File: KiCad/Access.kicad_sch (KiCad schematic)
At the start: 59 parts, among them J1 USB-C, J2 RFID, J3 INPUTS, J4 ExtTamper, J5 POWER, J6 DOOR, Q1 NX7002AK, SW1 Tamper, U1 ESP32-WROOM-32, U2 FT231XQ, U3 G3VM-41GR8, U4 LMR16006YQ3, U5 LMR16006YQ3/Q5, U6 AA, U7 QR

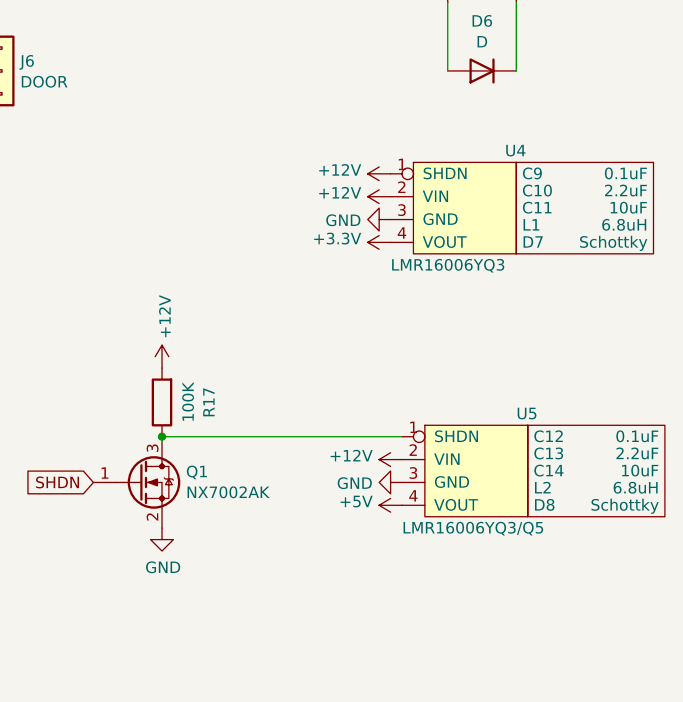
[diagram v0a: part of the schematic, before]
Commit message: More KiCad 6 tweaks
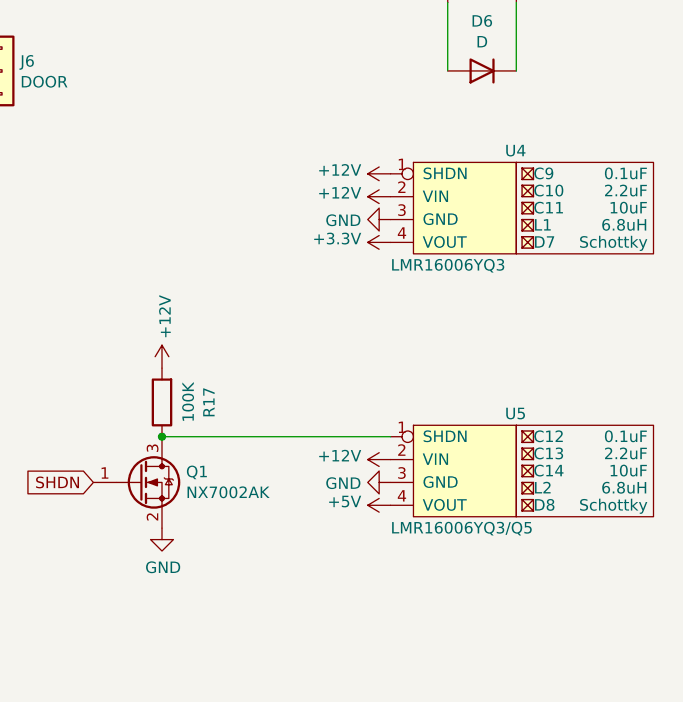
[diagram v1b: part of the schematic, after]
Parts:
- D1, D2, D3, D4: footprint Package_TO_SOT_SMD:SOT-363_SC-70-6 -> RevK:SOT-363_SC-70-6
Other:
- moved on the sheet: U5

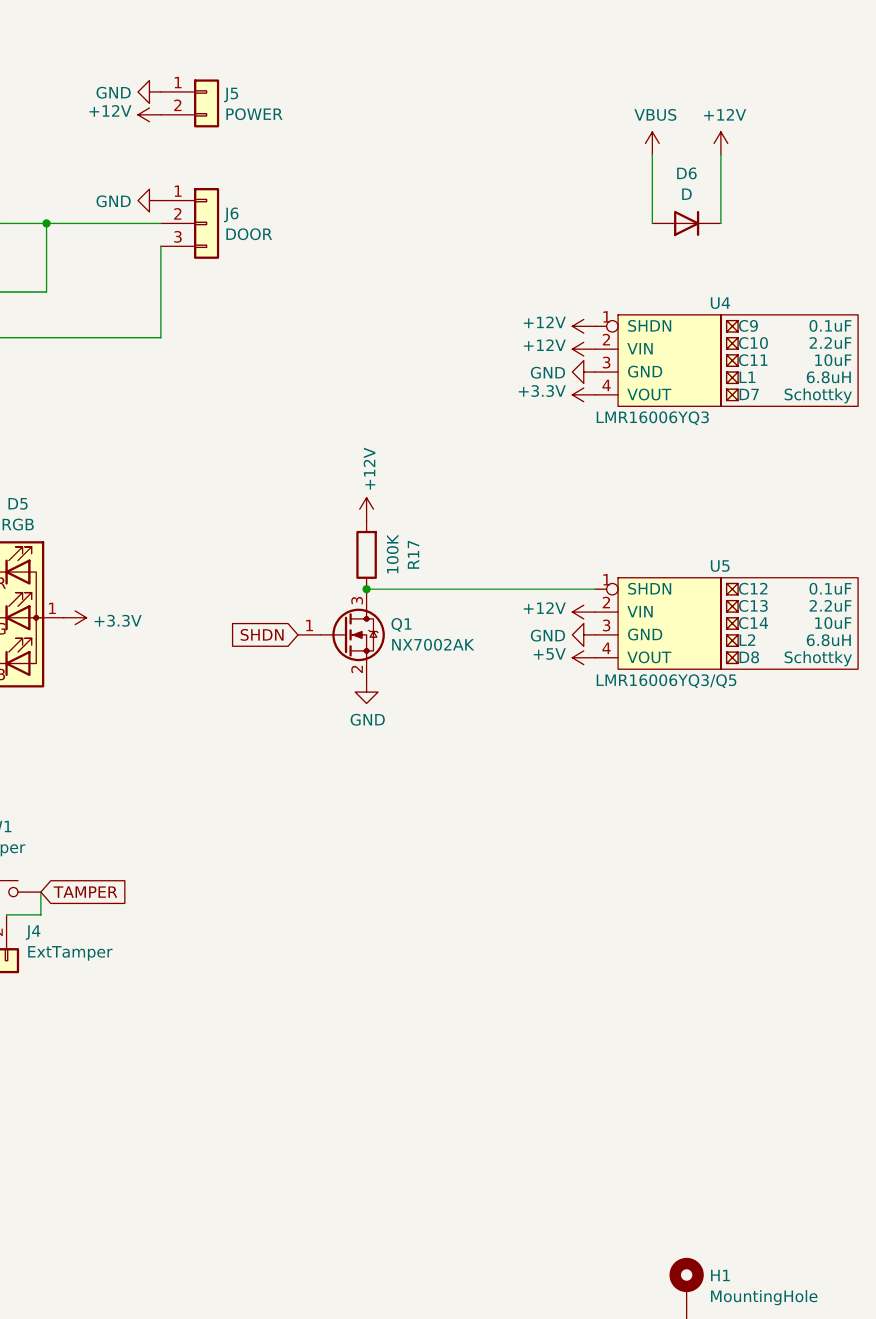
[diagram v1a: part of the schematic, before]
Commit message: Reworked for variable regulators
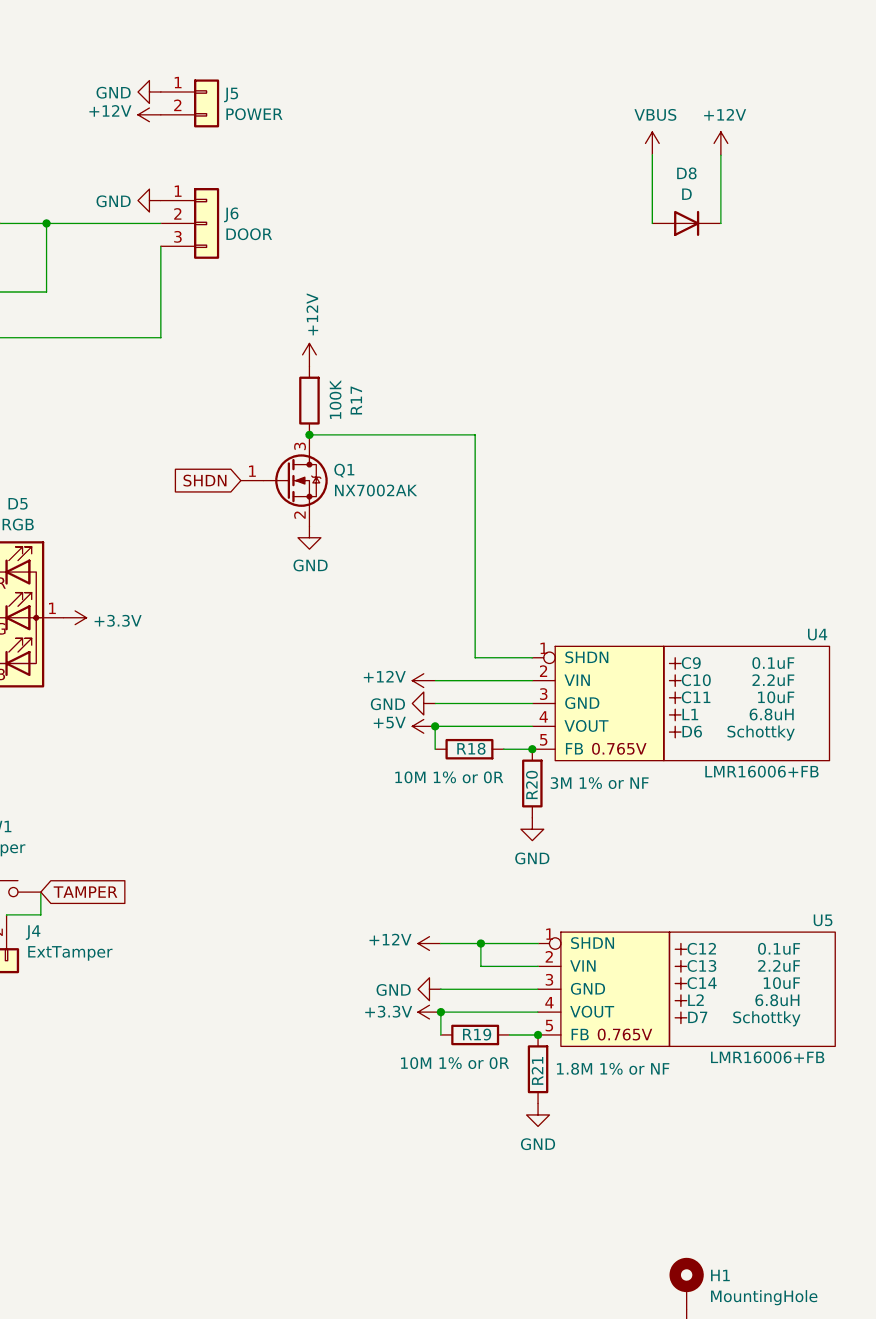
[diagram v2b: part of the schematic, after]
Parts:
- removed U4: LMR16006YQ3, RevK:RegulatorBlock, symbol RevK:LMR16006YQ3
- removed U5: LMR16006YQ3/Q5, RevK:RegulatorBlock, symbol RevK:LMR16006YQ3
- added R18, R19: 10M 1% or 0R, RevK:R_0603, symbol Device:R
- added R20: 3M 1% or NF, RevK:R_0603, symbol Device:R
- added R21: 1.8M 1% or NF, RevK:R_0603, symbol Device:R
- added U4, U5: LMR16006+FB, RevK:RegulatorBlockFB, symbol RevK:LMR16006+FB
- AJK1, U6, U7: Note (none) -> Non part, PCB printed
- D1, D2, D3, D4: footprint RevK:SOT-363_SC-70-6 -> Package_TO_SOT_SMD:SOT-363_SC-70-6
- renumbered C13 to C10, C14 to C11, C9 to C12, C10 to C13, C11 to C14, C12 to C9, D8 to D6, D6 to D8, L2 to L1, L1 to L2
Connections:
- net +12V: now also U4.2 (VIN), U5.1 (SHDN), U5.2 (VIN)
- net +3V3: now also R19.1, U5.4 (VOUT)
- net +5V: now also R18.1, U4.4 (VOUT)
- net GND: now also R20.1, R21.1, U4.3 (GND), U5.3 (GND)
- net at Q1.3 (D), R17.1: now also U4.1 (SHDN)
- new net: R19.2, R21.2, U5.5 (FB)
- new net: R18.2, R20.2, U4.5 (FB)
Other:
- moved on the sheet: Q1, R17

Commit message: Update date, and tidy
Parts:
- U1: footprint RF_Module:ESP32-WROOM-32 -> RevK:ESP32-WROOM-32
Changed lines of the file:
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@@
     (property "Reference" "U1" (id 0) (at 46.99 22.7076 0))
     (property "Value" "ESP32-WROOM-32" (id 1) (at 46.99 25.019 0))
-    (property "Footprint" "RF_Module:ESP32-WROOM-32" (id 2) (at 46.99 100.965 0)
+    (property "Footprint" "RevK:ESP32-WROOM-32" (id 2) (at 46.99 100.965 0)
       (effects (font (size 1.27 1.27)) hide)
     )
@@
     )
     (path "/00000000-0000-0000-0000-00006043326c"
-      (reference "U1") (unit 1) (value "ESP32-WROOM-32") (footprint "RF_Module:ESP32-WROOM-32")
+      (reference "U1") (unit 1) (value "ESP32-WROOM-32") (footprint "RevK:ESP32-WROOM-32")
     )
     (path "/00000000-0000-0000-0000-00006084108b"

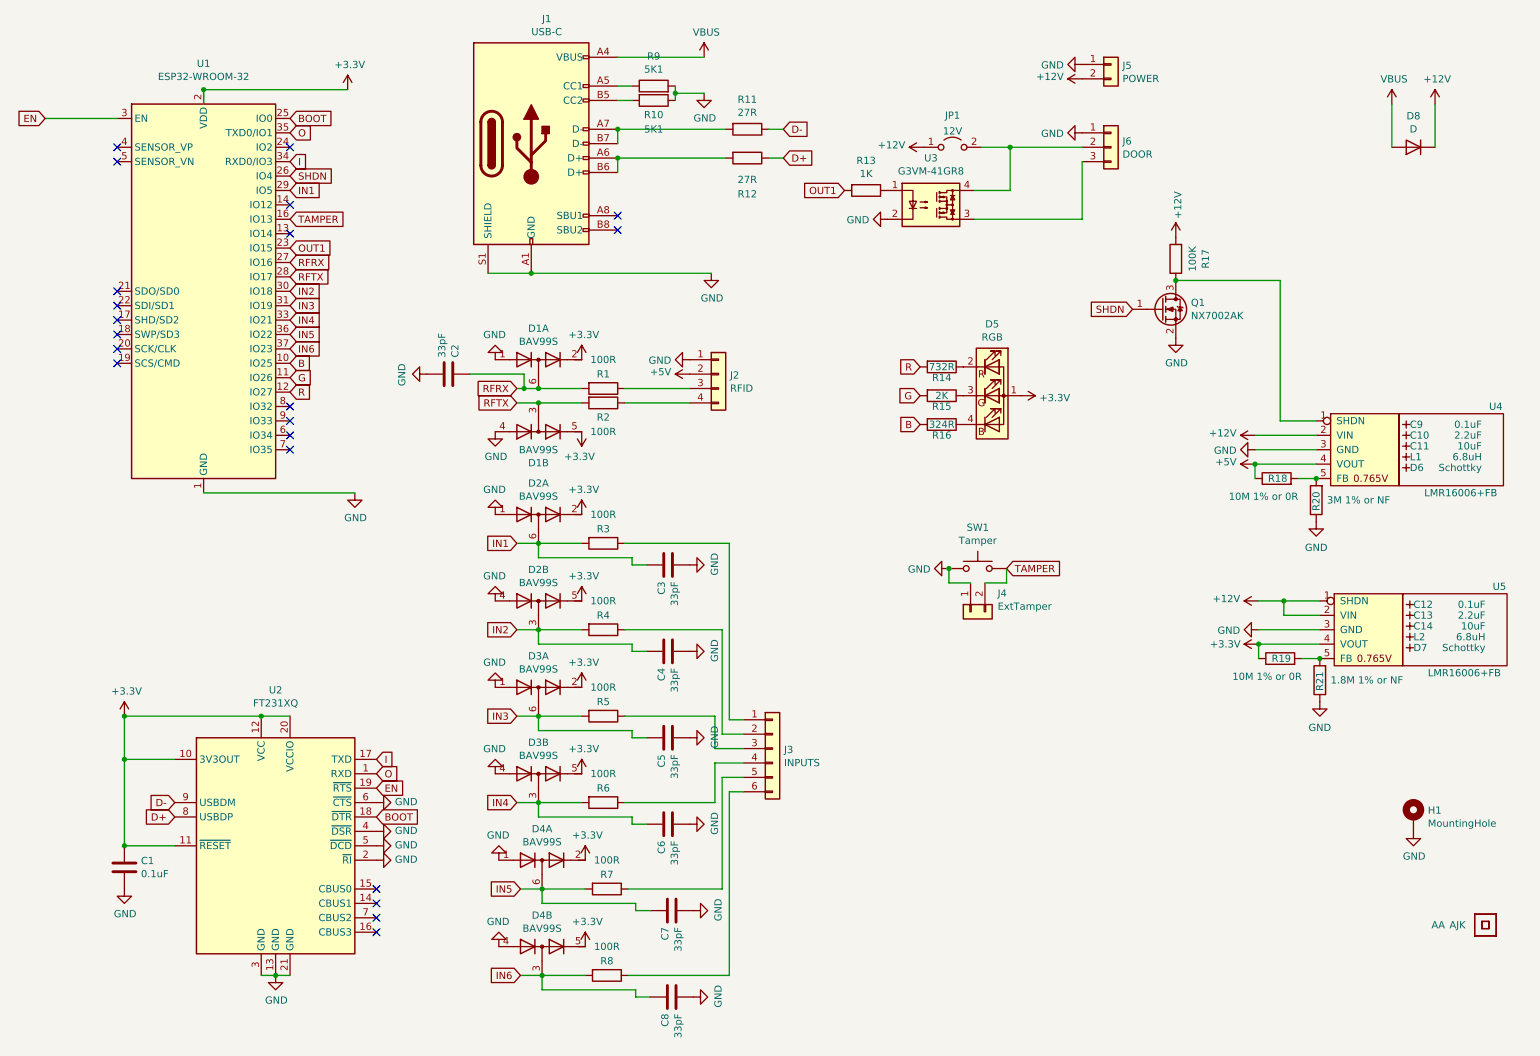
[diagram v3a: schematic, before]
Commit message: Updated for VBUS and GPIO changes
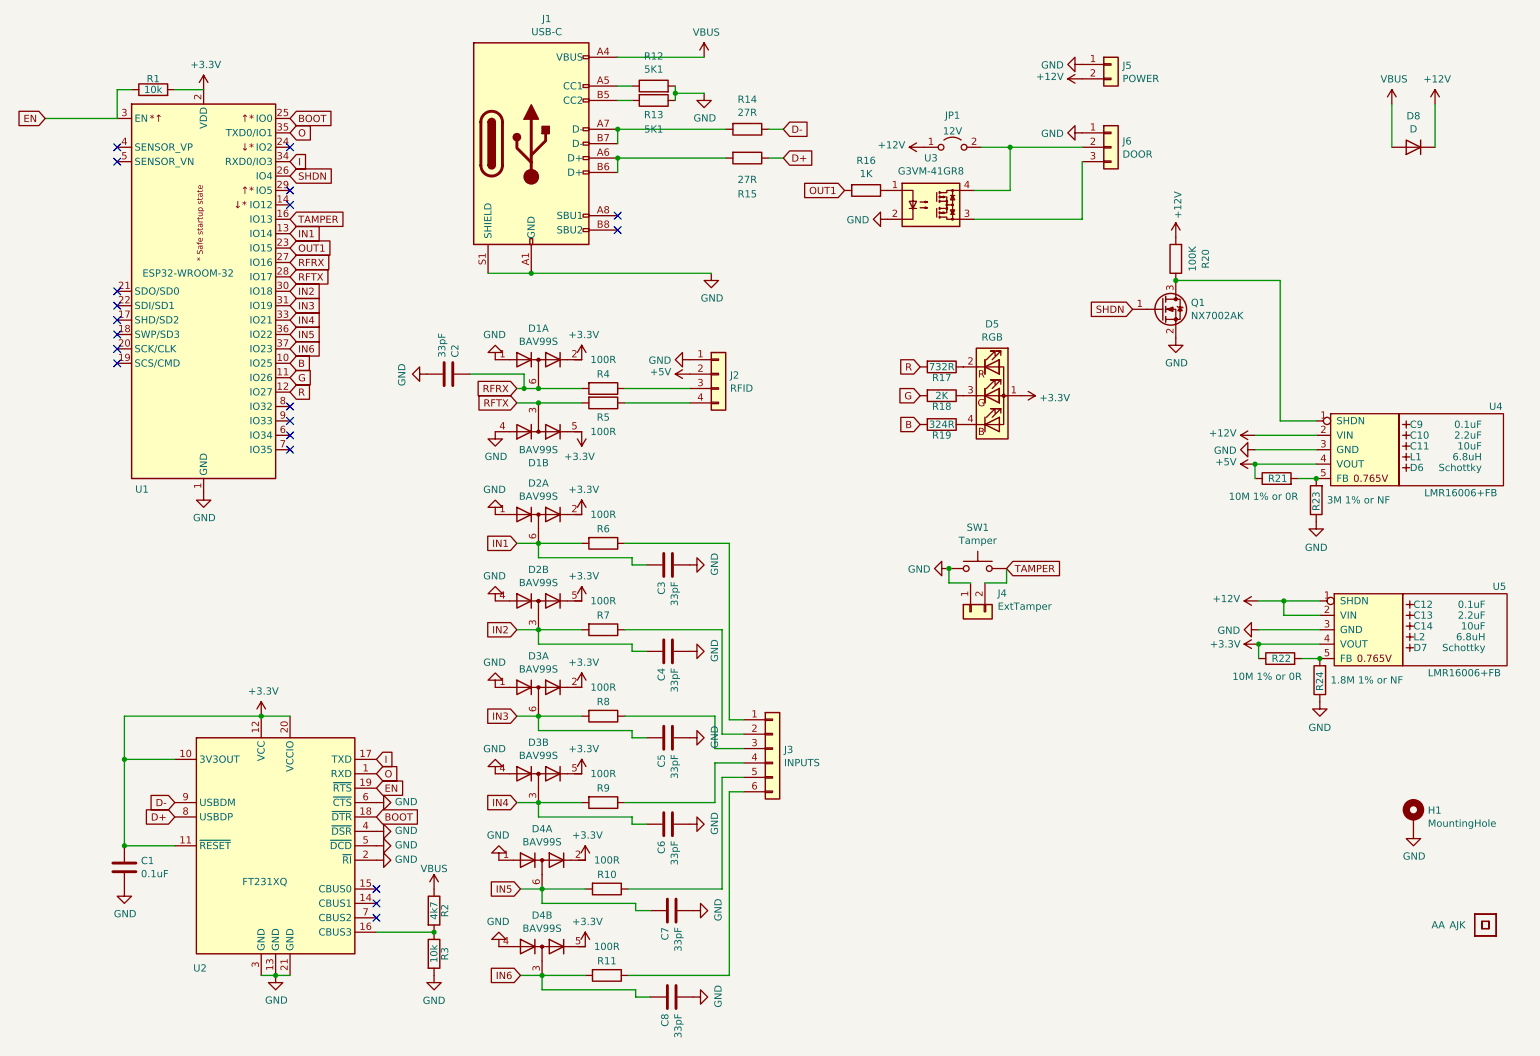
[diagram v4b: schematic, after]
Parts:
- removed U1: ESP32-WROOM-32, RevK:ESP32-WROOM-32, symbol RF_Module:ESP32-WROOM-32
- added R1, R3: 10k, RevK:R_0603, symbol Device:R
- added R2: 4k7, RevK:R_0603, symbol Device:R
- added U1: ESP32-WROOM-32, RevK:ESP32-WROOM-32, symbol RevK:ESP32-WROOM-32
- renumbered R7 to R10, R8 to R11, R9 to R12, R10 to R13, R11 to R14, R12 to R15, R13 to R16, R14 to R17, R15 to R18, R16 to R19, R17 to R20, R18 to R21, R19 to R22, R20 to R23, R21 to R24, R1 to R4, R2 to R5, R3 to R6, R4 to R7, R5 to R8, R6 to R9
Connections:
- net +3V3: now also R1.2, U1.2 (VDD)
- net B: now also U1.10 (IO25)
- net BOOT: now also U1.25 (IO0)
- net EN: now also R1.1, U1.3 (EN)
- net G: now also U1.11 (IO26)
- net GND: now also R3.2, U1.1 (GND), U1.15 (GND), U1.38 (GND), U1.39 (GND)
- net I: now also U1.34 (RXD0/IO3)
- net IN1: now also U1.13 (IO14)
- net IN2: now also U1.30 (IO18)
- net IN3: now also U1.31 (IO19)
- net IN4: now also U1.33 (IO21)
- net IN5: now also U1.36 (IO22)
- net IN6: now also U1.37 (IO23)
- net O: now also U1.35 (TXD0/IO1)
- net OUT1: now also U1.23 (IO15)
- net R: now also U1.12 (IO27)
- net RFRX: now also U1.27 (IO16)
- net RFTX: now also U1.28 (IO17)
- net SHDN: now also U1.26 (IO4)
- net TAMPER: now also U1.16 (IO13)
- net VBUS: now also R2.1
- net at U2.16 (CBUS3): now also R2.2, R3.1
- no-connect marks 21 -> 20

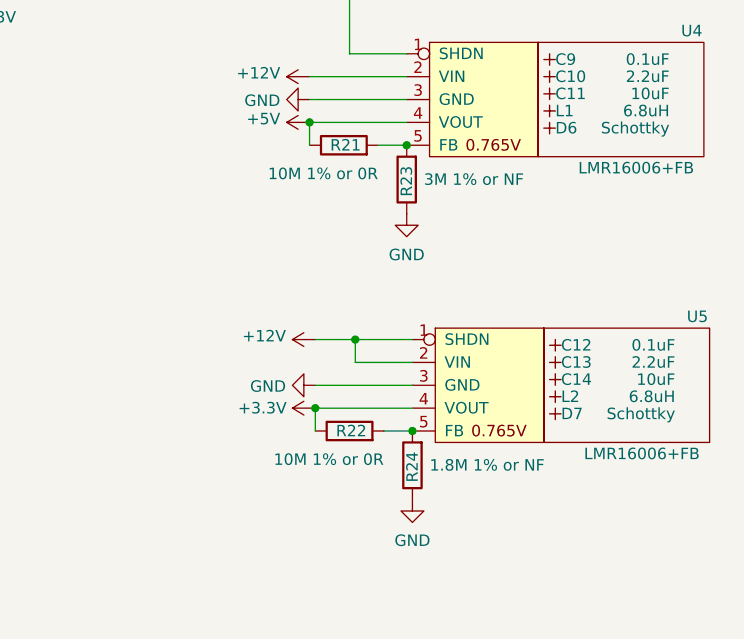
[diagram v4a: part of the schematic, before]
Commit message: Resistor fixes
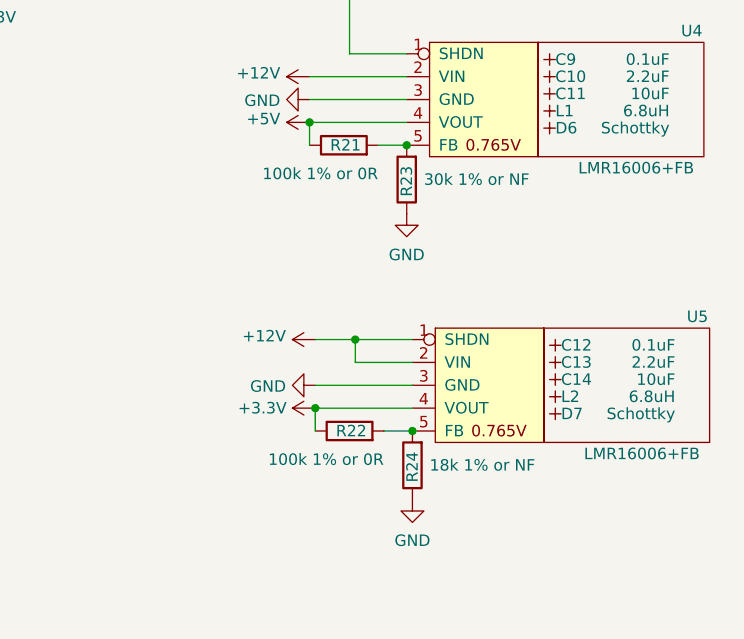
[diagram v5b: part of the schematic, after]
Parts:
- R21, R22: value 10M 1% or 0R -> 100k 1% or 0R
- R23: value 3M 1% or NF -> 30k 1% or NF
- R24: value 1.8M 1% or NF -> 18k 1% or NF
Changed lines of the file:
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@@
       (effects (font (size 1.27 1.27)) (justify left))
     )
-    (property "Value" "10M 1% or 0R" (id 1) (at 240.03 99.06 90)
+    (property "Value" "100k 1% or 0R" (id 1) (at 240.03 99.06 90)
       (effects (font (size 1.27 1.27)) (justify left))
     )
@@
       (effects (font (size 1.27 1.27)) (justify left))
     )
-    (property "Value" "10M 1% or 0R" (id 1) (at 240.665 130.81 90)
+    (property "Value" "100k 1% or 0R" (id 1) (at 240.665 130.81 90)
       (effects (font (size 1.27 1.27)) (justify left))
     )
@@
       (effects (font (size 1.27 1.27)) (justify right))
     )
-    (property "Value" "1.8M 1% or NF" (id 1) (at 245.745 131.445 0)
+    (property "Value" "18k 1% or NF" (id 1) (at 245.745 131.445 0)
       (effects (font (size 1.27 1.27)) (justify right))
     )
@@
       (effects (font (size 1.27 1.27)) (justify right))
     )
-    (property "Value" "3M 1% or NF" (id 1) (at 245.11 99.695 0)
+    (property "Value" "30k 1% or NF" (id 1) (at 245.11 99.695 0)
       (effects (font (size 1.27 1.27)) (justify right))
     )
@@
     )
     (path "/0a7f75d0-9f86-4caa-a0e4-44ff4b8f6861"
-      (reference "R21") (unit 1) (value "10M 1% or 0R") (footprint "RevK:R_0603")
+      (reference "R21") (unit 1) (value "100k 1% or 0R") (footprint "RevK:R_0603")
     )
     (path "/0d353d81-a7d7-4ff0-89eb-60271d9c4a01"
-      (reference "R22") (unit 1) (value "10M 1% or 0R") (footprint "RevK:R_0603")
+      (reference "R22") (unit 1) (value "100k 1% or 0R") (footprint "RevK:R_0603")
     )
     (path "/d571cde4-c062-4e90-8e0a-c6147d1b6cd4"
-      (reference "R23") (unit 1) (value "3M 1% or NF") (footprint "RevK:R_0603")
+      (reference "R23") (unit 1) (value "30k 1% or NF") (footprint "RevK:R_0603")
     )
     (path "/8271dfba-3962-4c80-a371-fd4d42efa2fe"
-      (reference "R24") (unit 1) (value "1.8M 1% or NF") (footprint "RevK:R_0603")
+      (reference "R24") (unit 1) (value "18k 1% or NF") (footprint "RevK:R_0603")
     )
     (path "/00000000-0000-0000-0000-00006093be97"
